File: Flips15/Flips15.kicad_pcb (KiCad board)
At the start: 2 copper layers, 100 x 100 mm, 59 parts, among them CN1 UFP2810, U1001 74HC238, U1002 ULN2803A, U1003 74HC238, U1004 TBD62783A, U1101 74HC238, U1102 ULN2803A, U1103 74HC238, U1104 TBD62783A, U701 74HC238, U801 74HC238, U802 ULN2803A, U803 74HC238, U804 TBD62783A, U901 74HC238, U902 ULN2803A, U903 74HC238, U904 TBD62783A

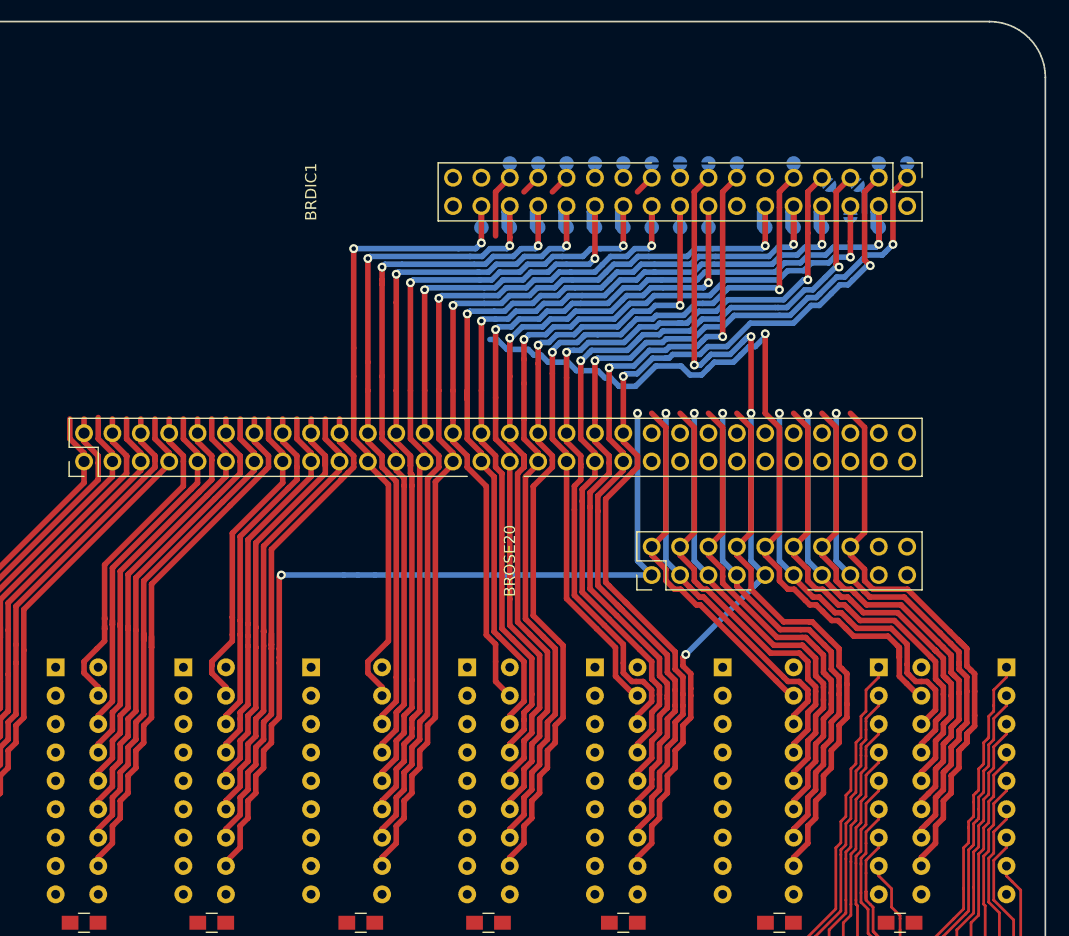
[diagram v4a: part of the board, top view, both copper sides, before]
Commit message: more traces for flips15
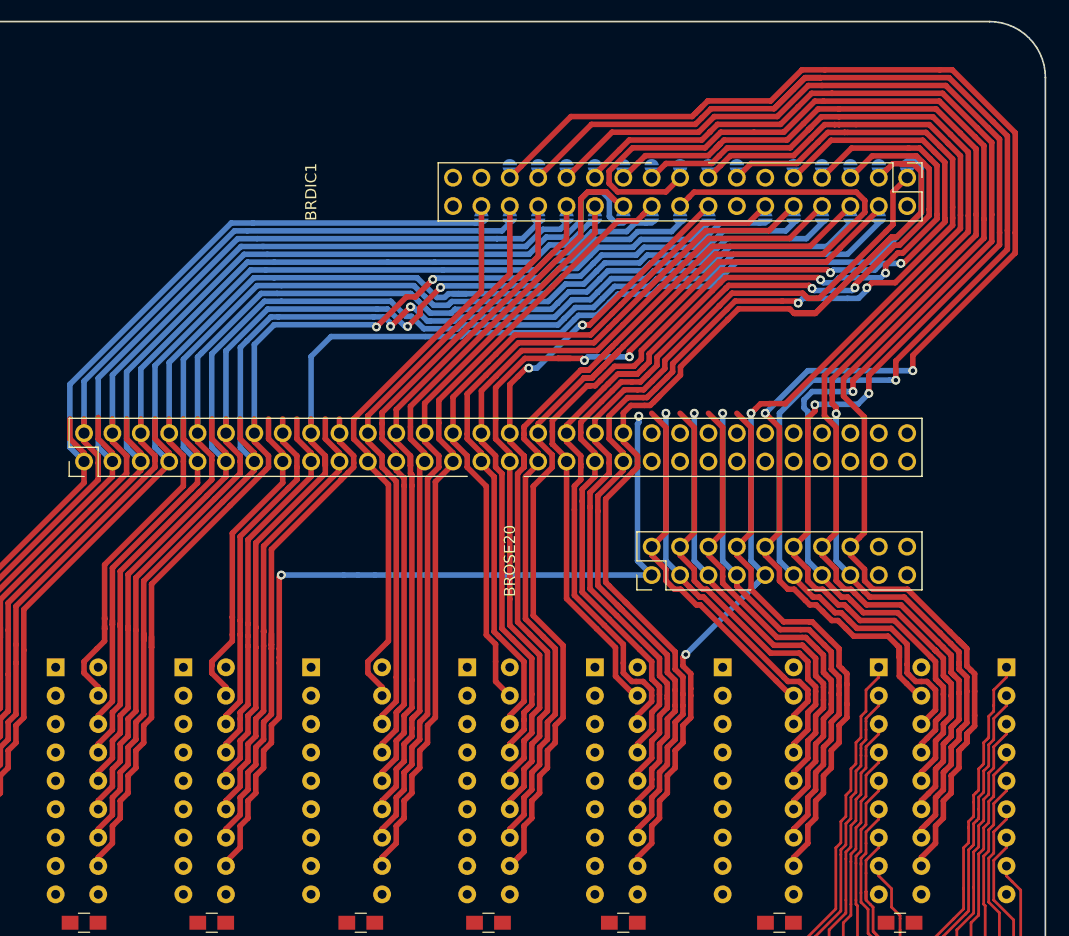
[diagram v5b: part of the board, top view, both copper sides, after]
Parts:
- moved JP117 1.77 mm to (133.3, 63.8), turned to 270 degrees
- moved JP116 1.77 mm to (130.8, 63.8), turned to 270 degrees
- moved JP101 0.89 mm to (100.3, 68.3), turned to 90 degrees
- moved JP102 0.89 mm to (102.9, 68.3), turned to 90 degrees
- moved JP103 0.89 mm to (105.4, 68.3), turned to 90 degrees
- moved JP104 0.89 mm to (108.0, 68.3), turned to 90 degrees
- moved JP105 0.89 mm to (113.0, 68.3), turned to 90 degrees
- moved JP106 0.89 mm to (110.5, 68.3), turned to 90 degrees
- moved JP107 0.89 mm to (115.6, 68.3), turned to 90 degrees
- moved JP108 0.89 mm to (125.7, 68.3), turned to 90 degrees
- moved JP109 0.89 mm to (128.3, 68.3), turned to 90 degrees
- moved JP110 0.89 mm to (130.8, 68.3), turned to 90 degrees
- moved JP111 0.89 mm to (135.9, 68.3), turned to 90 degrees
- moved JP112 0.89 mm to (120.7, 68.3), turned to 90 degrees
- moved JP114 0.89 mm to (118.1, 68.3), turned to 90 degrees
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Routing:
- net /X23: track 39.7 -> 127.9 mm
- net /SY11: track 37.8 -> 114.6 mm
- net /X24: track 42.8 -> 117.7 mm, vias 0 -> 2
- net /X28: track 52.0 -> 126.7 mm
- net /X25: track 43.2 -> 116.6 mm
- net /SY18: track 37.5 -> 109.9 mm
- net /SY13: track 44.4 -> 116.2 mm, vias 0 -> 2
- net /SY9: track 31.9 -> 102.7 mm
- net /SY10: track 34.8 -> 105.2 mm
- net /SY8: track 29.9 -> 97.4 mm
- net /X27: track 47.2 -> 111.7 mm
- net /SY5: track 42.4 -> 105.3 mm
- net /SY7: track 47.9 -> 106.7 mm
- net /X26: track 48.0 -> 106.3 mm
- net /SY12: track 40.7 -> 97.9 mm, vias 0 -> 2
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
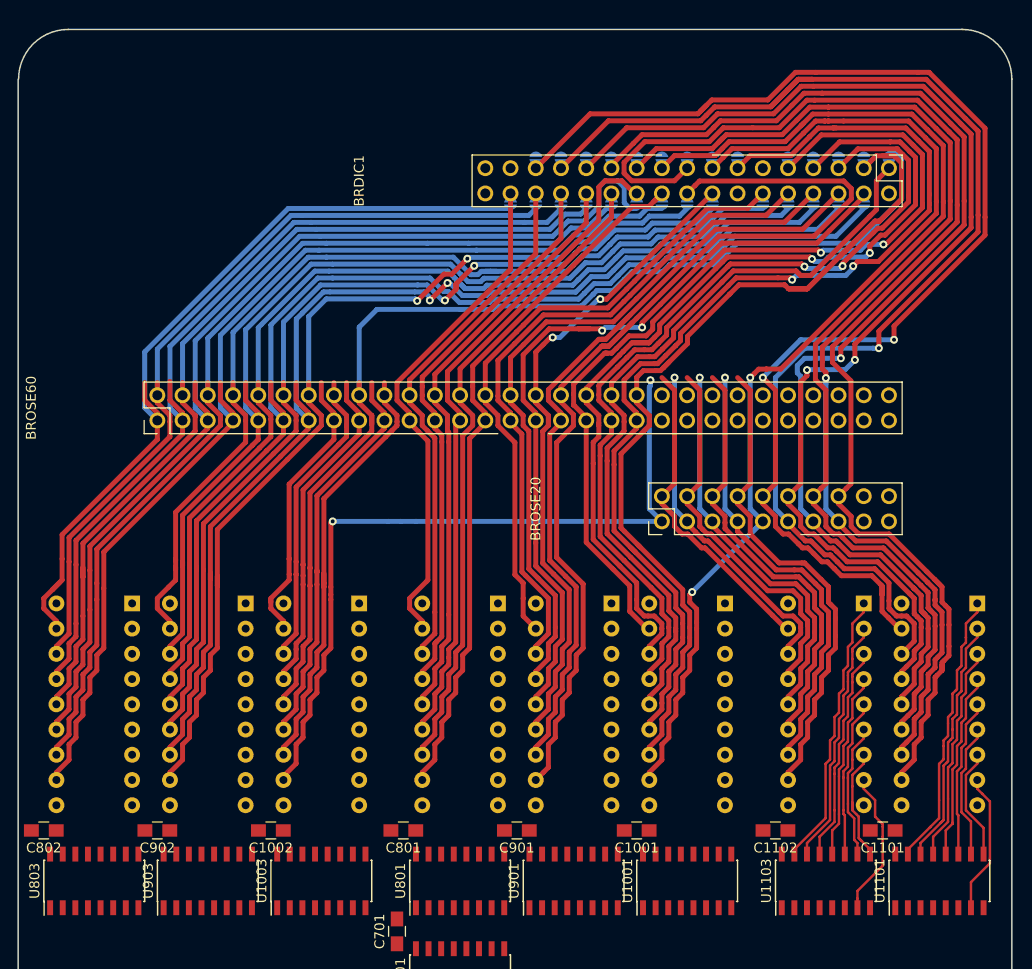
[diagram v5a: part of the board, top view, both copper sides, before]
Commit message: more tracing in flips15
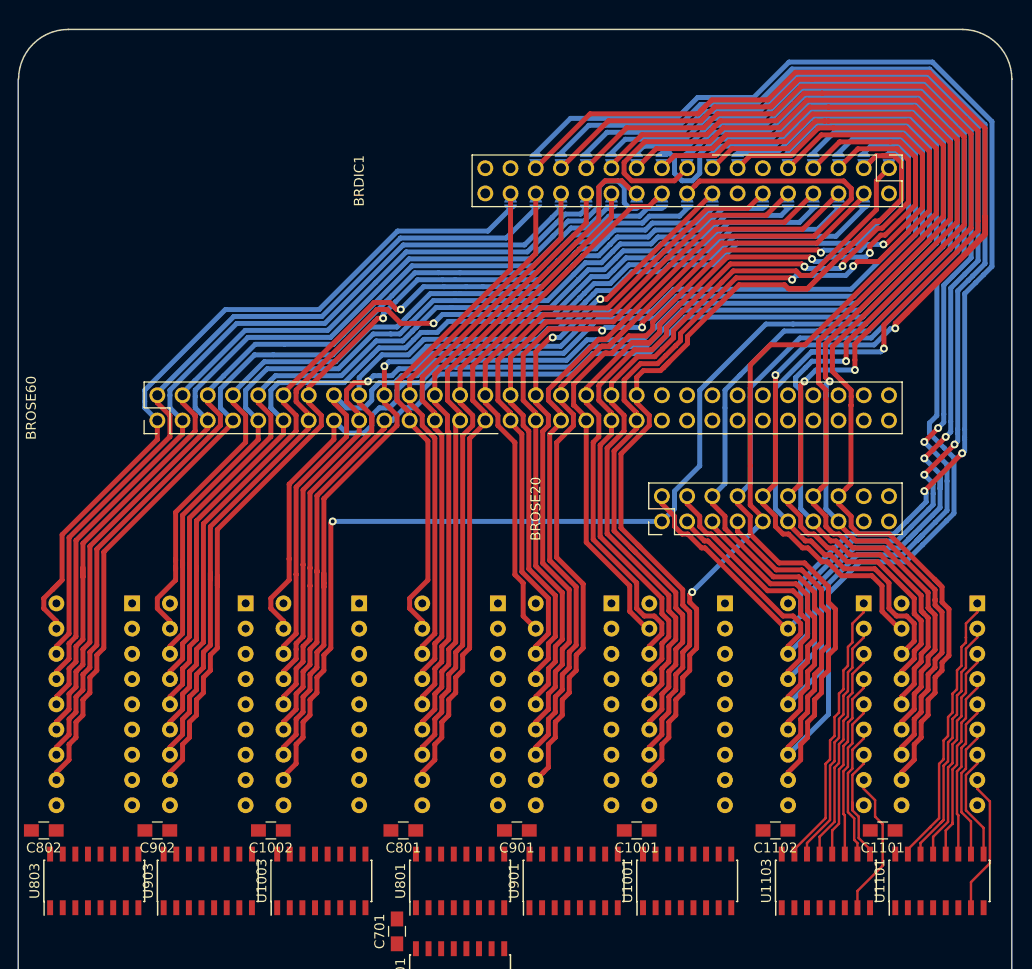
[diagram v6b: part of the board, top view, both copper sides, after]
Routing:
- net /SY22: track 32.3 -> 134.6 mm, vias 0 -> 2
- net /SY24: track 39.0 -> 140.7 mm, vias 0 -> 2
- net /SY23: track 34.4 -> 132.8 mm, vias 1 -> 2
- net /SY27: track 45.5 -> 142.5 mm, vias 1 -> 0
- net /SY25: track 40.3 -> 137.2 mm, vias 1 -> 2
- net /SY19: track 39.8 -> 131.8 mm
- net /SY15: track 28.7 -> 119.9 mm
- net /SY16: track 30.5 -> 118.1 mm
- net /SY17: track 33.5 -> 113.6 mm, vias 0 -> 1
- net /SY20: track 44.1 -> 118.9 mm, vias 0 -> 1
- net /SY26: track 43.9 -> 118.7 mm
- net /SY28: track 49.1 -> 116.9 mm
- net /SY21: track 76.0 -> 143.4 mm, vias 2 -> 1
- net /X22: track 128.1 -> 140.4 mm
- net /SY11: track 114.6 -> 104.3 mm
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
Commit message: adding fill for flips15
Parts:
- moved CN1 130.0 mm to (121.9, 146.1), turned to 270 degrees
- moved BROSE34 77.4 mm to (116.8, 54.6), turned to 270 degrees
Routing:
- added copper zone on B.Cu, net GND
- added copper zone on F.Cu, net GND

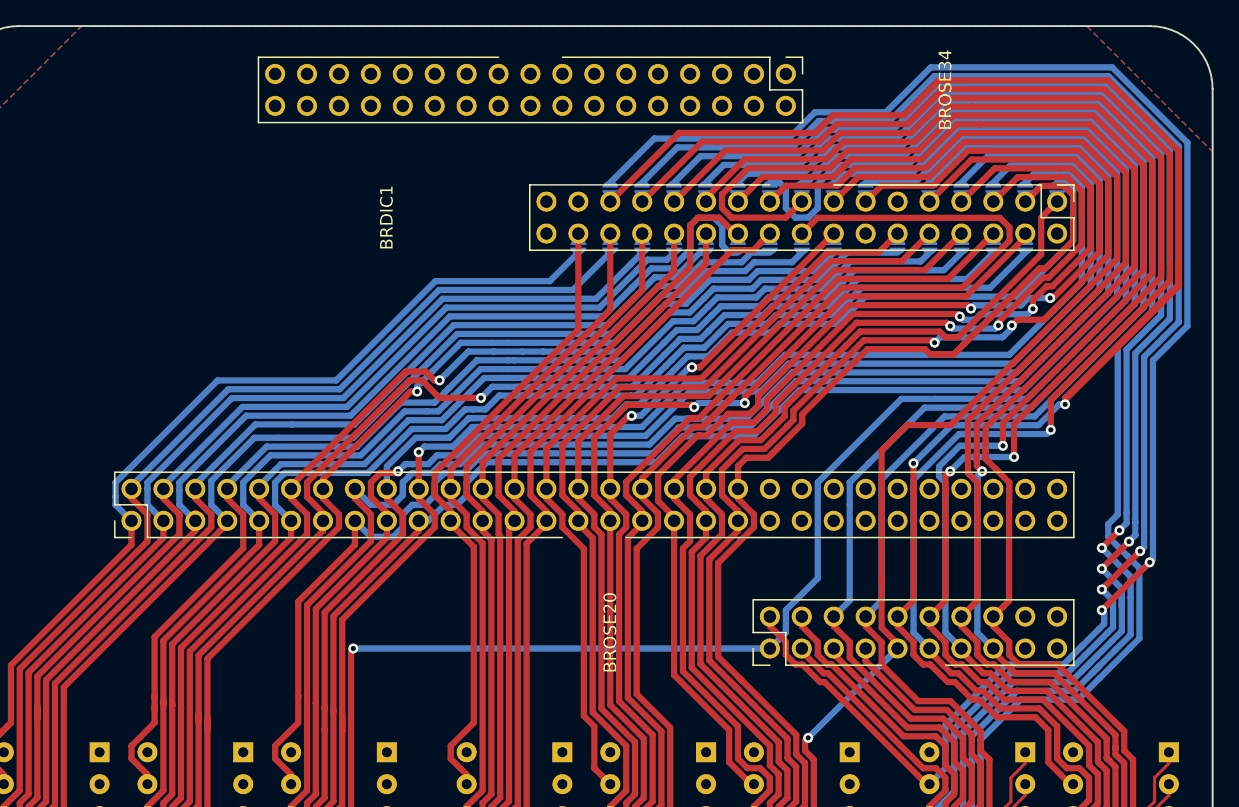
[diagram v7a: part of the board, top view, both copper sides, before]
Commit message: more tracing with overlapping connectors
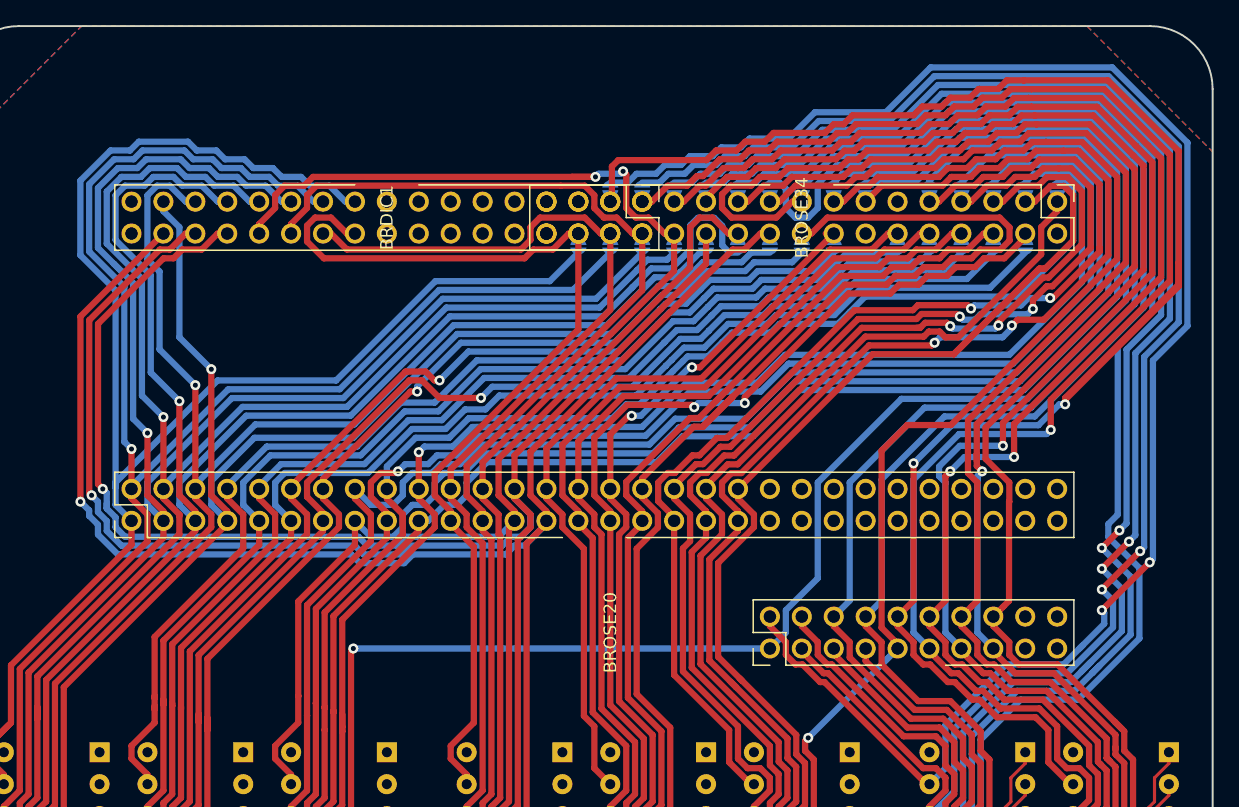
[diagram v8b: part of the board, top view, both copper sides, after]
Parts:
- moved BROSE34 15.3 mm to (105.4, 64.8)
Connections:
- BRDIC1 pad 31: Net-(BRDIC1-Pad31) -> /T5
- BRDIC1 pad 33: Net-(BRDIC1-Pad33) -> /T7
- BRDIC1 pad 34: Net-(BRDIC1-Pad34) -> /T8
- BROSE34 pad 1: Net-(BROSE34-Pad1) -> /X23
- BROSE34 pad 2: Net-(BROSE34-Pad2) -> /X3
- BROSE34 pad 3: Net-(BROSE34-Pad3) -> /X22
- BROSE34 pad 4: Net-(BROSE34-Pad4) -> /X2
- BROSE34 pad 5: Net-(BROSE34-Pad5) -> /T5
- BROSE34 pad 6: Net-(BROSE34-Pad6) -> /X1
- BROSE34 pad 7: Net-(BROSE34-Pad7) -> /T7
- BROSE34 pad 8: Net-(BROSE34-Pad8) -> /T8
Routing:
- net /X6: track 65.5 -> 133.1 mm, vias 0 -> 1
- net /X7: track 72.2 -> 136.5 mm, vias 0 -> 1
- net /X5: track 67.6 -> 131.2 mm, vias 0 -> 1
- net /SY1: track 75.3 -> 125.9 mm
- net /SY3: track 81.8 -> 129.1 mm, vias 0 -> 1
- net /SY2: track 77.3 -> 124.4 mm, vias 0 -> 1
- net /X4: track 59.4 -> 100.6 mm, vias 0 -> 2
- net /SY4: track 87.1 -> 126.6 mm, vias 0 -> 1
- net /SY5: track 98.0 -> 136.9 mm, vias 0 -> 1
- net /X3: track 56.3 -> 89.0 mm
- net /SY6: track 92.2 -> 121.8 mm, vias 0 -> 1
- net /X1: track 51.1 -> 80.0 mm
- net /SY7: track 99.2 -> 126.7 mm, vias 0 -> 1
- net /X2: track 53.2 -> 78.8 mm
- net /X20: track 104.6 -> 97.7 mm
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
